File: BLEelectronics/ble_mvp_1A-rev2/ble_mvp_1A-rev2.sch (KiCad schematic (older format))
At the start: 19 parts, among them IC1 LTC4412xS6, IC2 PCF8523T, IC3 MX25R6435FM2IL0, J1 Nordic_nRF52840_breakout, Q1 Si2307CDS, U1 LP5907MFX-3.3, U2 BAT-HLD-001, U3 ESD401, U4 ESD401, X1 32.768KHZ

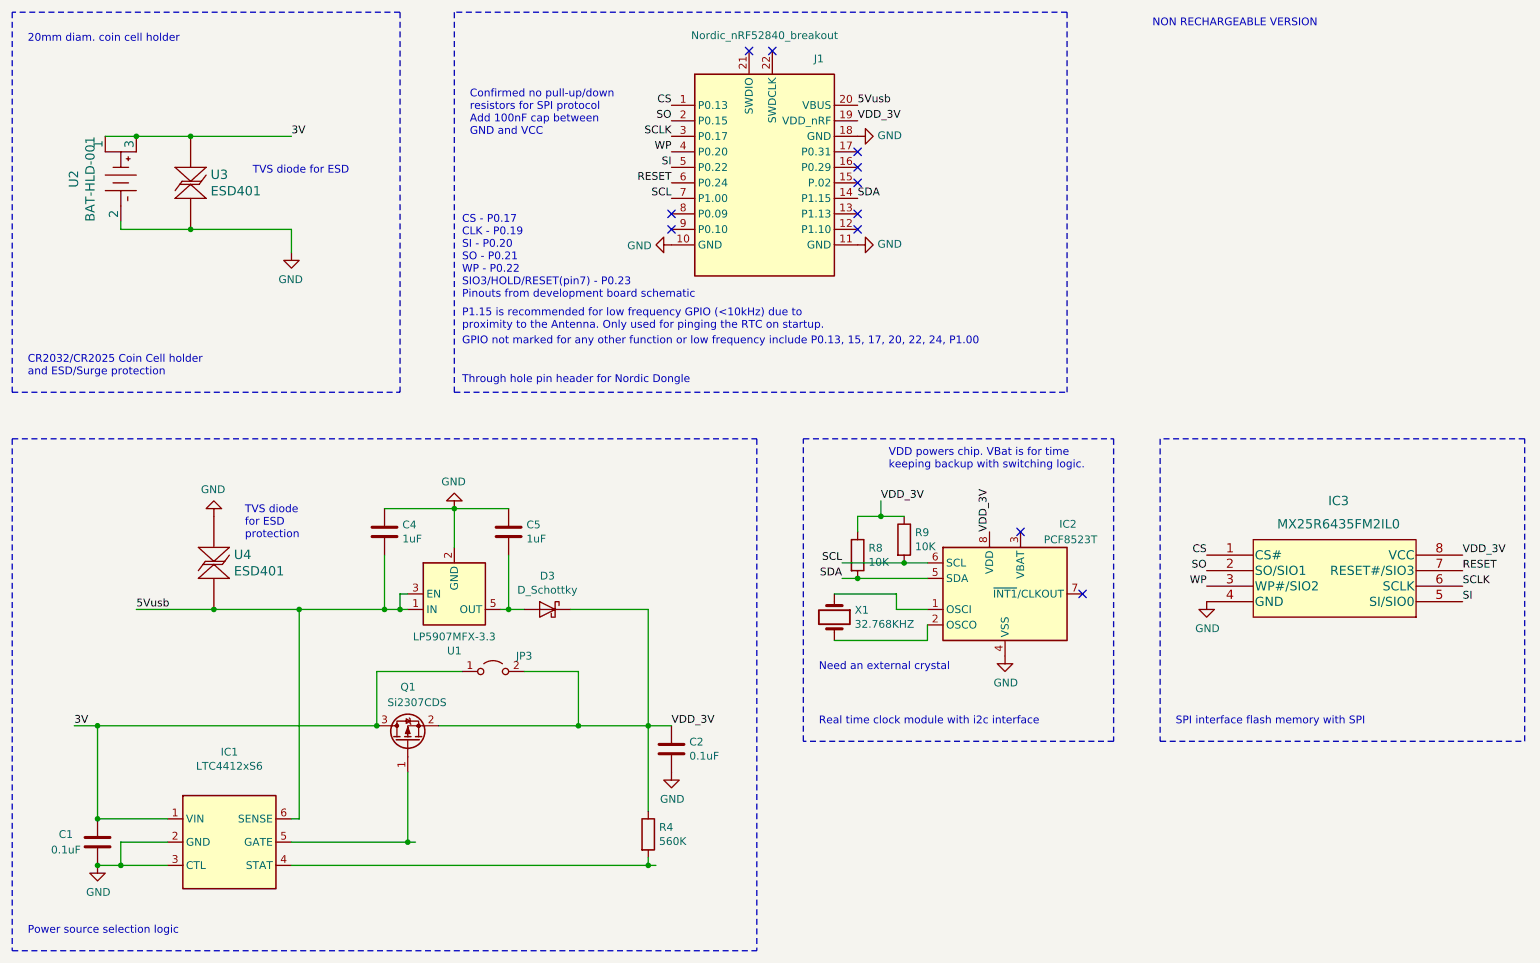
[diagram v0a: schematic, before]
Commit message: MVP1A-rev2 ready for fab/assembly. DRC clean, .pos clean, BOM clean.
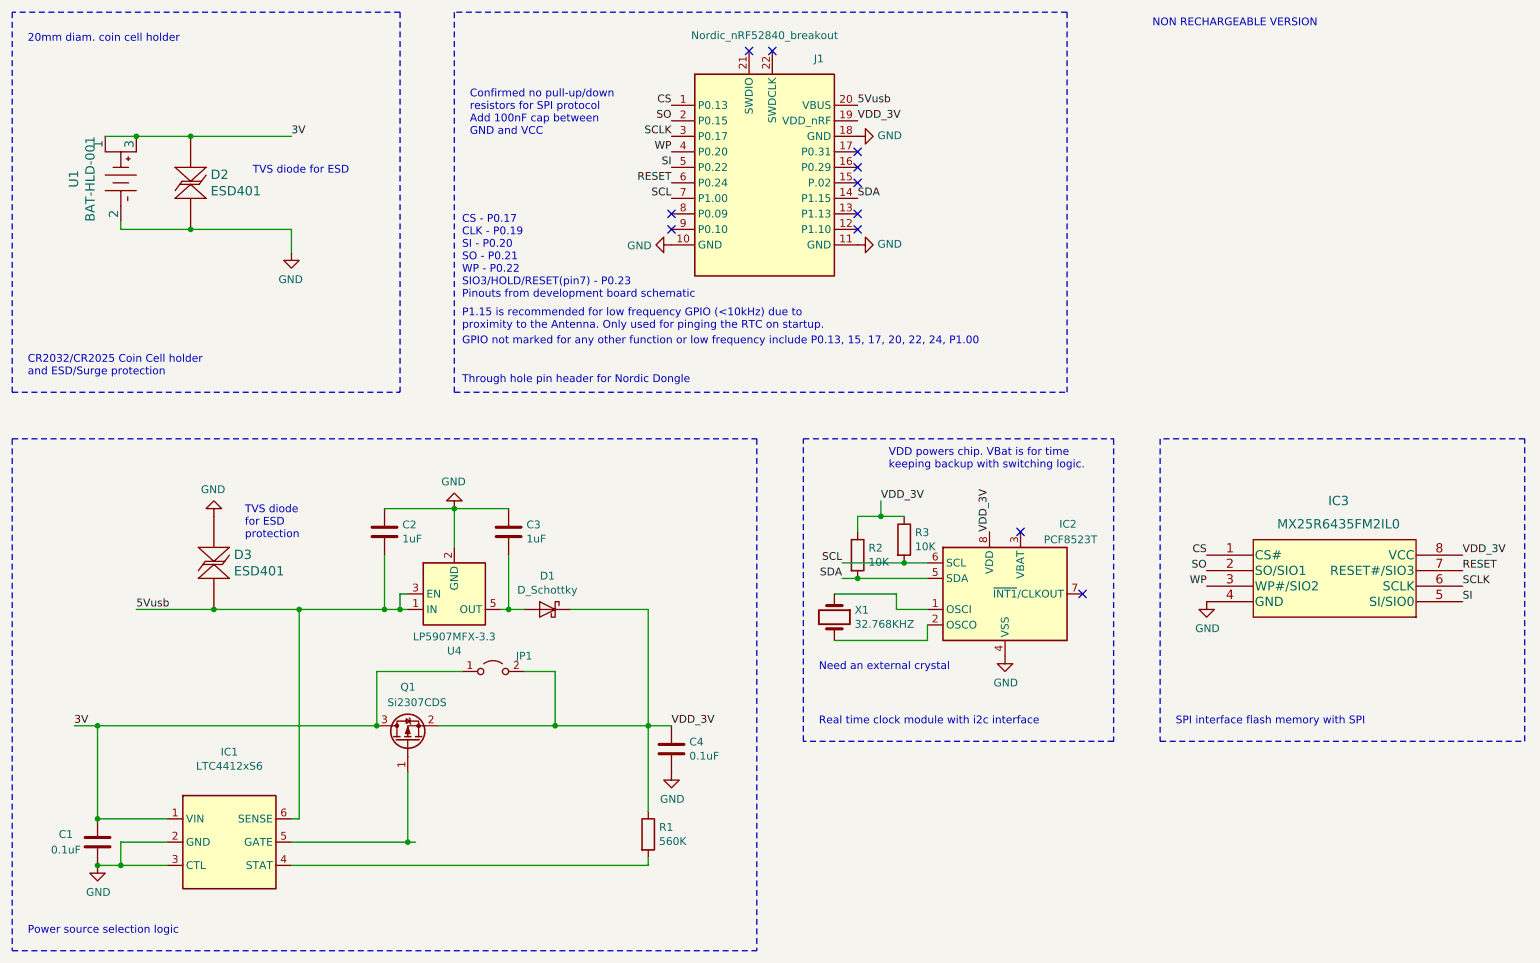
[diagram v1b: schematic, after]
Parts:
- renumbered C4 to C2, C5 to C3, C2 to C4, D3 to D1, U3 to D2, U4 to D3, JP3 to JP1, R4 to R1, R8 to R2, R9 to R3, U2 to U1, U1 to U4
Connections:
- wire segments 60 -> 59
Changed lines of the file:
@@
 $EndDescr
 $Comp
-L BAT-HLD-001:BAT-HLD-001 U2
+L BAT-HLD-001:BAT-HLD-001 U1
 U 1 1 5E9C706C
 P 1650 1700
-F 0 "U2" H 1925 1903 60  0000 C CNN
+F 0 "U1" H 1925 1903 60  0000 C CNN
 F 1 "BAT-HLD-001" H 1925 1797 60  0000 C CNN
 F 2 "0my_footprints:BAT-HLD-001" H 1934 1358 60  0001 C CNN
@@
 $EndComp
 $Comp
-L power:GND #PWR01
+L power:GND #PWR03
 U 1 1 5E9D6756
 P 2850 2450
-F 0 "#PWR01" H 2850 2200 50  0001 C CNN
+F 0 "#PWR03" H 2850 2200 50  0001 C CNN
 F 1 "GND" H 2855 2277 50  0000 C CNN
 F 2 "" H 2850 2450 50  0001 C CNN
@@
 $EndComp
 $Comp
-L power:GND #PWR09
+L power:GND #PWR07
 U 1 1 5EA74258
 P 6500 1700
-F 0 "#PWR09" H 6500 1450 50  0001 C CNN
+F 0 "#PWR07" H 6500 1450 50  0001 C CNN
 F 1 "GND" V 6505 1572 50  0000 R CNN
 F 2 "" H 6500 1700 50  0001 C CNN
@@
 $EndComp
 $Comp
-L power:GND #PWR010
+L power:GND #PWR08
 U 1 1 5EA75FDA
 P 6500 2400
-F 0 "#PWR010" H 6500 2150 50  0001 C CNN
+F 0 "#PWR08" H 6500 2150 50  0001 C CNN
 F 1 "GND" V 6505 2272 50  0000 R CNN
 F 2 "" H 6500 2400 50  0001 C CNN
@@
 $EndComp
 $Comp
-L power:GND #PWR08
+L power:GND #PWR05
 U 1 1 5EA772EE
 P 5300 2400
-F 0 "#PWR08" H 5300 2150 50  0001 C CNN
+F 0 "#PWR05" H 5300 2150 50  0001 C CNN
 F 1 "GND" V 5305 2272 50  0000 R CNN
 F 2 "" H 5300 2400 50  0001 C CNN
@@
 $EndComp
 $Comp
-L power:GND #PWR0101
+L power:GND #PWR09
 U 1 1 5EA0EA9A
 P 7450 5050
-F 0 "#PWR0101" H 7450 4800 50  0001 C CNN
+F 0 "#PWR09" H 7450 4800 50  0001 C CNN
 F 1 "GND" H 7455 4877 50  0000 C CNN
 F 2 "" H 7450 5050 50  0001 C CNN
@@
 $EndComp
 $Comp
-L Device:R R9
+L Device:R R3
 U 1 1 5EA074F4
 P 6800 4300
-F 0 "R9" H 6870 4346 50  0000 L CNN
+F 0 "R3" H 6870 4346 50  0000 L CNN
 F 1 "10K" H 6870 4255 50  0000 L CNN
 F 2 "Resistor_SMD:R_0603_1608Metric_Pad1.05x0.95mm_HandSolder" V 6730 4300 50  0001 C CNN
@@
 $EndComp
 $Comp
-L Device:R R8
+L Device:R R2
 U 1 1 5EA0D031
 P 6500 4400
-F 0 "R8" H 6570 4446 50  0000 L CNN
+F 0 "R2" H 6570 4446 50  0000 L CNN
 F 1 "10K" H 6570 4355 50  0000 L CNN
 F 2 "Resistor_SMD:R_0603_1608Metric_Pad1.05x0.95mm_HandSolder" V 6430 4400 50  0001 C CNN
@@
 F 1 "0.1uF" H 1300 6200 50  0000 L CNN
 F 2 "Capacitor_SMD:C_0603_1608Metric_Pad1.05x0.95mm_HandSolder" H 1638 6100 50  0001 C CNN
-F 3 "~" H 1600 6250 50  0001 C CNN
+F 3 "https://www.yageo.com/upload/media/product/productsearch/datasheet/mlcc/UPY-GPHC_X7R_6.3V-to-50V_18.pdf" H 1600 6250 50  0001 C CNN
 F 4 "Yageo" H -3000 3750 50  0001 C CNN "MFR"
 F 5 "CC0603KRX7R9BB104" H -3000 3750 50  0001 C CNN "MPN"
@@
 $EndComp
 $Comp
-L power:GND #PWR03
+L power:GND #PWR01
 U 1 1 5E9D9BC8
 P 1600 6400
-F 0 "#PWR03" H 1600 6150 50  0001 C CNN
+F 0 "#PWR01" H 1600 6150 50  0001 C CNN
 F 1 "GND" H 1605 6227 50  0000 C CNN
 F 2 "" H 1600 6400 50  0001 C CNN
@@
 $EndComp
 $Comp
-L Device:C C2
+L Device:C C4
 U 1 1 5E9D2D00
 P 5300 5650
-F 0 "C2" H 5415 5696 50  0000 L CNN
+F 0 "C4" H 5415 5696 50  0000 L CNN
 F 1 "0.1uF" H 5415 5605 50  0000 L CNN
 F 2 "Capacitor_SMD:C_0603_1608Metric_Pad1.05x0.95mm_HandSolder" H 5338 5500 50  0001 C CNN
-F 3 "~" H 5300 5650 50  0001 C CNN
+F 3 "https://www.yageo.com/upload/media/product/productsearch/datasheet/mlcc/UPY-GPHC_X7R_6.3V-to-50V_18.pdf" H 5300 5650 50  0001 C CNN
 F 4 "Yageo" H -1700 3750 50  0001 C CNN "MFR"
 F 5 "CC0603KRX7R9BB104" H -1700 3750 50  0001 C CNN "MPN"
@@
 $EndComp
 $Comp
-L power:GND #PWR04
+L power:GND #PWR06
 U 1 1 5E9D3A19
 P 5300 5800
-F 0 "#PWR04" H 5300 5550 50  0001 C CNN
+F 0 "#PWR06" H 5300 5550 50  0001 C CNN
 F 1 "GND" H 5305 5627 50  0000 C CNN
 F 2 "" H 5300 5800 50  0001 C CNN
@@
 $EndComp
 $Comp
-L Device:R R4
+L Device:R R1
 U 1 1 5E9D42B2
 P 5150 6200
-F 0 "R4" H 5220 6246 50  0000 L CNN
+F 0 "R1" H 5220 6246 50  0000 L CNN
 F 1 "560K" H 5220 6155 50  0000 L CNN
 F 2 "Resistor_SMD:R_0603_1608Metric_Pad1.05x0.95mm_HandSolder" V 5080 6200 50  0001 C CNN
-F 3 "~" H 5150 6200 50  0001 C CNN
+F 3 "https://www.yageo.com/upload/media/product/productsearch/datasheet/rchip/PYu-RC_Group_51_RoHS_L_10.pdf" H 5150 6200 50  0001 C CNN
 F 4 "Yageo" H -1700 3750 50  0001 C CNN "MFR"
 F 5 "RC0201FR-07560KL" H -1700 3750 50  0001 C CNN "MPN"
@@
 $EndComp
 $Comp
-L Device:D_Schottky D3
+L Device:D_Schottky D1
 U 1 1 5E9EFF12
 P 4500 4750
-F 0 "D3" H 4500 4966 50  0000 C CNN
+F 0 "D1" H 4500 4966 50  0000 C CNN
 F 1 "D_Schottky" H 4500 4875 50  0000 C CNN
 F 2 "Diode_SMD:D_SOD-123F" H 4500 4750 50  0001 C CNN
@@
 $EndComp
 $Comp
-L Regulator_Linear:LP5907MFX-3.3 U1
+L Regulator_Linear:LP5907MFX-3.3 U4
 U 1 1 5EA3D589
 P 3900 4650
-F 0 "U1" H 3900 5017 50  0000 C CNN
+F 0 "U4" H 3900 5017 50  0000 C CNN
 F 1 "LP5907MFX-3.3" H 3900 4926 50  0000 C CNN
 F 2 "Package_TO_SOT_SMD:SOT-23-5" H 3900 5000 50  0001 C CNN
@@
 $EndComp
 $Comp
-L power:GND #PWR07
+L power:GND #PWR04
 U 1 1 5EA4312B
 P 3900 4100
-F 0 "#PWR07" H 3900 3850 50  0001 C CNN
+F 0 "#PWR04" H 3900 3850 50  0001 C CNN
 F 1 "GND" H 3905 3927 50  0000 C CNN
 F 2 "" H 3900 4100 50  0001 C CNN
@@
 $EndComp
 $Comp
-L Device:C C4
+L Device:C C2
 U 1 1 5EA4DCA4
 P 3450 4250
-F 0 "C4" H 3565 4296 50  0000 L CNN
+F 0 "C2" H 3565 4296 50  0000 L CNN
 F 1 "1uF" H 3565 4205 50  0000 L CNN
 F 2 "Capacitor_SMD:C_0603_1608Metric_Pad1.05x0.95mm_HandSolder" H 3488 4100 50  0001 C CNN
@@
 $EndComp
 $Comp
-L Device:C C5
+L Device:C C3
 U 1 1 5EA4EF46
 P 4250 4250
-F 0 "C5" H 4365 4296 50  0000 L CNN
+F 0 "C3" H 4365 4296 50  0000 L CNN
 F 1 "1uF" H 4365 4205 50  0000 L CNN
 F 2 "Capacitor_SMD:C_0603_1608Metric_Pad1.05x0.95mm_HandSolder" H 4288 4100 50  0001 C CNN
@@
 $EndComp
 $Comp
-L Jumper:Jumper_2_Open JP3
-U 1 1 5EA10100
-P 4150 5150
-F 0 "JP3" H 4350 5250 50  0000 C CNN
-F 1 "Jumper_2_Open" H 4150 5294 50  0001 C CNN
-F 2 "Jumper:SolderJumper-2_P1.3mm_Open_RoundedPad1.0x1.5mm" H 4150 5150 50  0001 C CNN
-F 3 "~" H 4150 5150 50  0001 C CNN
-F 4 "-" H -2550 3050 50  0001 C CNN "MFR"
-F 5 "-" H -2550 3050 50  0001 C CNN "MPN"
-F 6 "-" H -2550 3050 50  0001 C CNN "DPN"
-F 7 "-" H -2550 3050 50  0001 C CNN "LCSCPN"
-F 8 "-" H -2550 3050 50  0001 C CNN "SPR"
-F 9 "-" H -2550 3050 50  0001 C CNN "SPN"
-F 10 "-" H -2550 3050 50  0001 C CNN "SIM"
-	1    4150 5150
-	1    0    0    -1
-$EndComp
-$Comp
 L power:GND #PWR02
 U 1 1 5EA2FE2A
@@
 $EndComp
 $Comp
-L ESD401DPYR:ESD401DPYR U3
+L ESD401DPYR:ESD401DPYR D2
 U 1 1 5EA48F38
 P 2200 2000
-F 0 "U3" V 2253 1871 60  0000 R CNN
+F 0 "D2" V 2253 1871 60  0000 R CNN
 F 1 "ESD401" V 2147 1871 60  0000 R CNN
 F 2 "0my_footprints:ESD401DPYR" H 2200 1940 60  0001 C CNN
@@
 $EndComp
 $Comp
-L ESD401DPYR:ESD401DPYR U4
+L ESD401DPYR:ESD401DPYR D3
 U 1 1 5EA4E7E7
 P 2350 4450
-F 0 "U4" V 2403 4321 60  0000 R CNN
+F 0 "D3" V 2403 4321 60  0000 R CNN
 F 1 "ESD401" V 2297 4321 60  0000 R CNN
 F 2 "0my_footprints:ESD401DPYR" H 2350 4390 60  0001 C CNN
@@
 $EndComp
 $Comp
-L power:GND #PWR011
+L power:GND #PWR010
 U 1 1 5EA9F122
 P 8750 4700
-F 0 "#PWR011" H 8750 4450 50  0001 C CNN
+F 0 "#PWR010" H 8750 4450 50  0001 C CNN
 F 1 "GND" H 8755 4527 50  0000 C CNN
 F 2 "" H 8750 4700 50  0001 C CNN
@@
 	2850 6100 2900 6100
 Wire Wire Line
-	3400 5150 3950 5150
-Wire Wire Line
-	4350 5150 4700 5150
-Wire Wire Line
-	4700 5150 4700 5500
-Wire Wire Line
-	3400 5150 3400 5500
-Wire Wire Line
 	2850 6400 5150 6400
 Wire Wire Line
@@
 	2850 6250 3600 6250
 Wire Wire Line
-	3800 5500 4700 5500
-Wire Wire Line
 	2900 4750 3450 4750
 Wire Wire Line
-	5150 6400 5200 6400
-Wire Wire Line
 	3600 6250 3650 6250
 Wire Wire Line
@@
 	3600 5800 3600 6250
 Wire Wire Line
-	1600 5500 3400 5500
-Wire Wire Line
 	6950 4850 6950 4950
 Wire Wire Line
@@
 Wire Wire Line
 	2050 6400 1750 6400
-Wire Wire Line
-	4700 5500 5150 5500
 Wire Wire Line
 	4650 4750 5150 4750
@@
 Connection ~ 1600 5500
 Connection ~ 3600 6250
-Connection ~ 4700 5500
 Connection ~ 2900 4750
-Connection ~ 5150 6400
 Connection ~ 1600 6100
 Connection ~ 1600 6400
@@
 Connection ~ 2200 2300
 Connection ~ 2200 1700
-Connection ~ 3400 5500
 Connection ~ 1750 6400
 NoConn ~ 5300 2300
@@
 Wire Notes Line
 	1050 3650 1050 6950
+Connection ~ 3400 5500
+Wire Wire Line
+	3800 5500 4550 5500
+Wire Wire Line
+	1600 5500 3400 5500
+Wire Wire Line
+	3400 5150 3400 5500
+Wire Wire Line
+	4550 5150 4550 5500
+Wire Wire Line
+	4350 5150 4550 5150
+Wire Wire Line
+	3400 5150 3950 5150
+$Comp
+L Jumper:Jumper_2_Open JP1
+U 1 1 5EA10100
+P 4150 5150
+F 0 "JP1" H 4350 5250 50  0000 C CNN
+F 1 "Jumper_2_Open" H 4150 5294 50  0001 C CNN
+F 2 "Jumper:SolderJumper-2_P1.3mm_Open_RoundedPad1.0x1.5mm" H 4150 5150 50  0001 C CNN
+F 3 "~" H 4150 5150 50  0001 C CNN
+F 4 "-" H -2550 3050 50  0001 C CNN "MFR"
+F 5 "-" H -2550 3050 50  0001 C CNN "MPN"
+F 6 "-" H -2550 3050 50  0001 C CNN "DPN"
+F 7 "-" H -2550 3050 50  0001 C CNN "LCSCPN"
+F 8 "-" H -2550 3050 50  0001 C CNN "SPR"
+F 9 "-" H -2550 3050 50  0001 C CNN "SPN"
+F 10 "-" H -2550 3050 50  0001 C CNN "SIM"
+	1    4150 5150
+	1    0    0    -1
+$EndComp
+Connection ~ 4550 5500
+Wire Wire Line
+	4550 5500 5150 5500
 $EndSCHEMATC

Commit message: correct CS to CS# in schematic and pdfs for all mvps
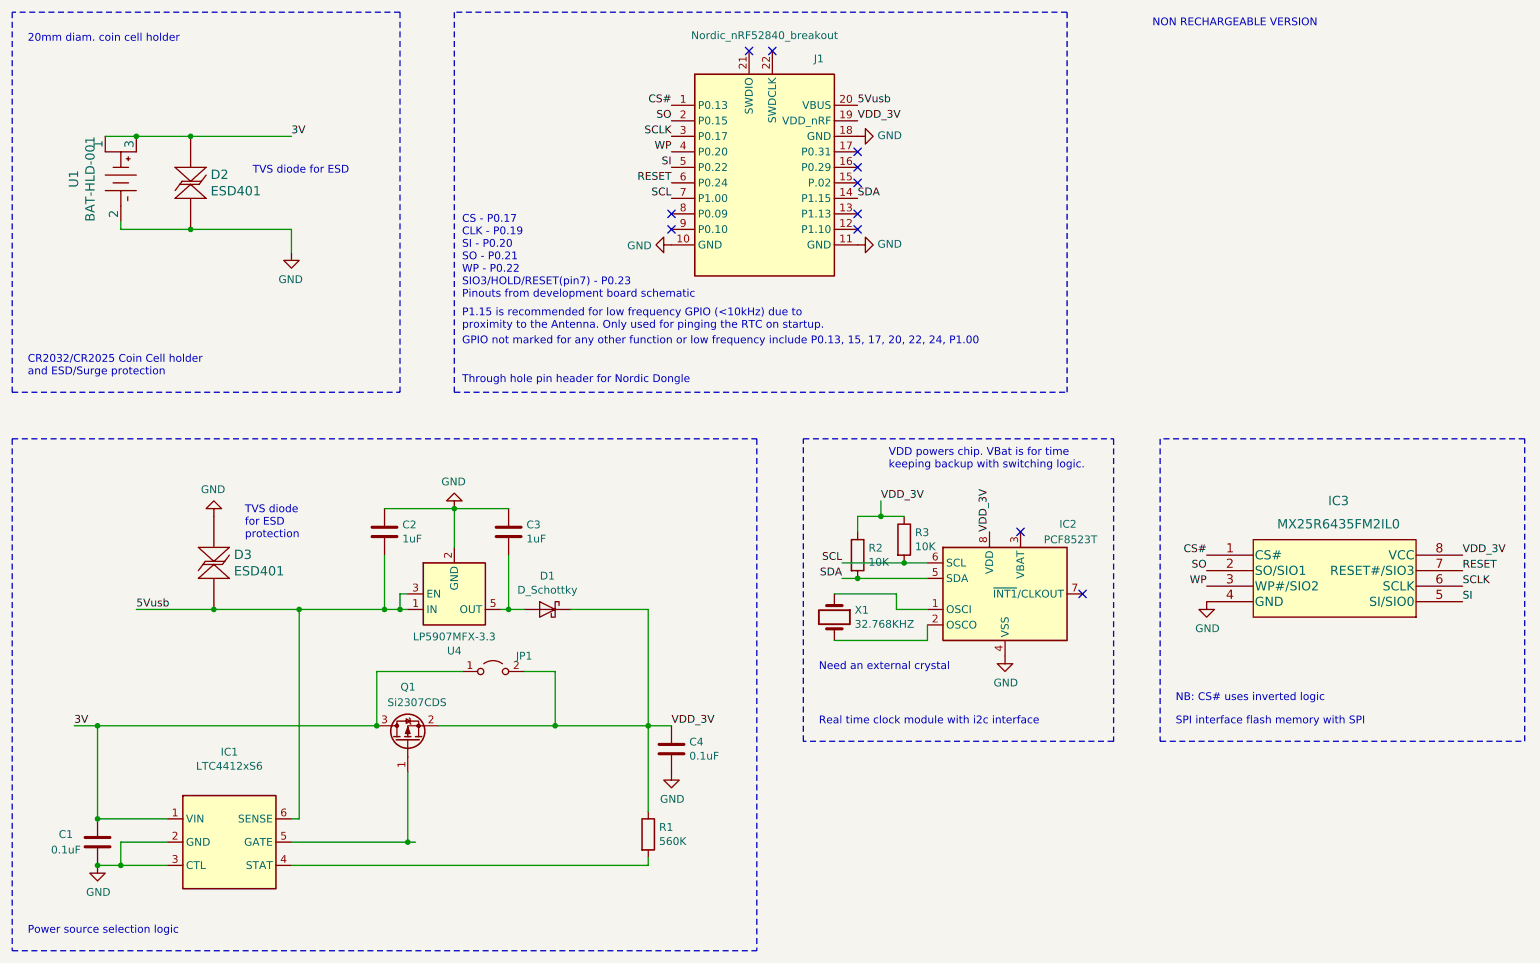
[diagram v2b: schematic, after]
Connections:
- net CS renamed CS#
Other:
- note added: "NB: CS# uses inverted logic"
- note removed: "Confirmed no pull-up/down\nresistors for SPI protocol\nAdd 100nF cap between \nGND and VCC"
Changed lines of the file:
@@
 RESET
 Text Label 8750 4400 2    50   ~ 0
-CS
+CS#
 Text Label 5300 1600 2    50   ~ 0
 SO
 Text Label 5300 1500 2    50   ~ 0
-CS
+CS#
 Text Label 5300 1900 2    50   ~ 0
 SI
@@
 Text Label 8750 4600 2    50   ~ 0
 WP
-Text Notes 4000 1700 0    50   ~ 0
-Confirmed no pull-up/down\nresistors for SPI protocol\nAdd 100nF cap between \nGND and VCC
 Text Label 6650 4050 0    50   ~ 0
 VDD_3V
@@
 Wire Wire Line
 	4550 5500 5150 5500
+Text Notes 8550 5350 0    50   ~ 0
+NB: CS# uses inverted logic
 $EndSCHEMATC
